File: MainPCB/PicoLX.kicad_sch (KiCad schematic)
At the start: 57 parts, among them J1 USB_C_Receptacle_USB2.0, SW1 SW_Push, U1 RP2040, U2 W25Q32JVSS, U3 NCP1117-3.3_SOT223, Y1 12.000MHz

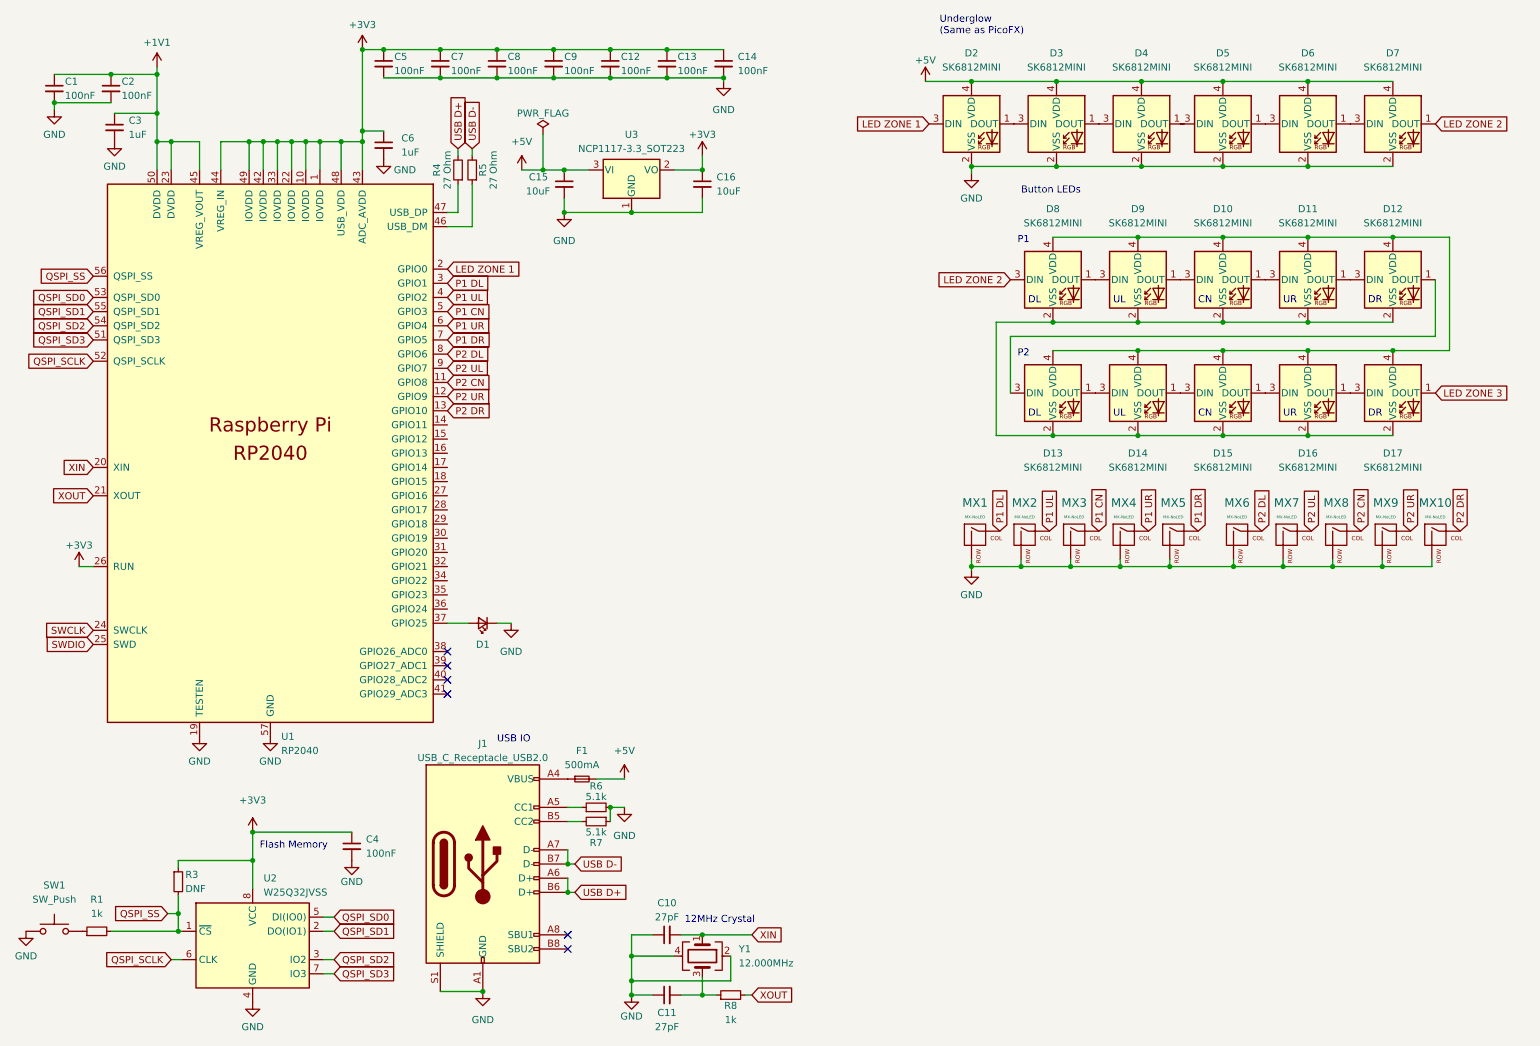
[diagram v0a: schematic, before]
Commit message: Route switches, begin routing LEDs
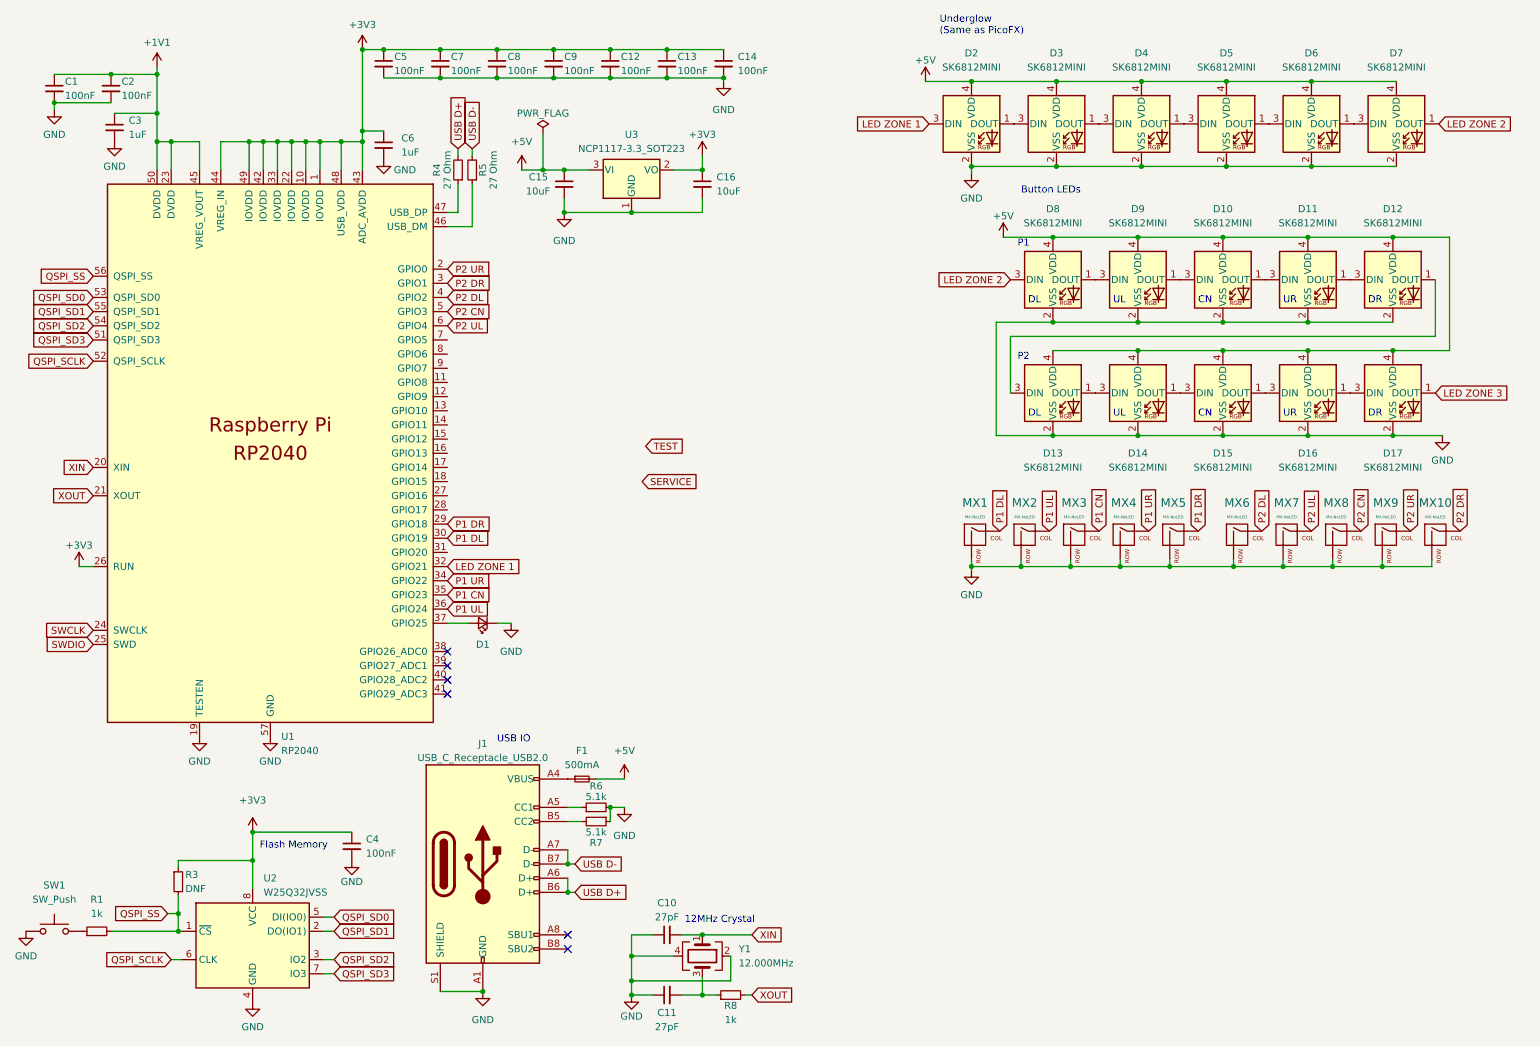
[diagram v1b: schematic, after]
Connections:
- net +5V: now also D10.4 (VDD), D11.4 (VDD), D12.4 (VDD), D13.4 (VDD), D14.4 (VDD), D15.4 (VDD), D16.4 (VDD), D17.4 (VDD), D8.4 (VDD), D9.4 (VDD)
- net GND: now also D10.2 (VSS), D11.2 (VSS), D12.2 (VSS), D13.2 (VSS), D14.2 (VSS), D15.2 (VSS), D16.2 (VSS), D17.2 (VSS), D8.2 (VSS), D9.2 (VSS)
- net LED ZONE 1: now also U1.32 (GPIO21); no longer U1.2 (GPIO0)
- net P1 CN: now also U1.35 (GPIO23); no longer U1.5 (GPIO3)
- net P1 DL: now also U1.30 (GPIO19); no longer U1.3 (GPIO1)
- net P1 DR: now also U1.29 (GPIO18); no longer U1.7 (GPIO5)
- net P1 UL: now also U1.36 (GPIO24); no longer U1.4 (GPIO2)
- net P1 UR: now also U1.34 (GPIO22); no longer U1.6 (GPIO4)
- net P2 CN: now also U1.5 (GPIO3); no longer U1.11 (GPIO8)
- net P2 DL: now also U1.4 (GPIO2); no longer U1.8 (GPIO6)
- net P2 DR: now also U1.3 (GPIO1); no longer U1.13 (GPIO10)
- net P2 UL: now also U1.6 (GPIO4); no longer U1.9 (GPIO7)
- net P2 UR: now also U1.2 (GPIO0); no longer U1.12 (GPIO9)
- net at D5.3 (DIN): now also D4.1 (DOUT)
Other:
- moved on the sheet: D5, D6, D7

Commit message: Final functional routing
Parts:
- added C17: 100nF, Capacitor_SMD:C_0402_1005Metric_Pad0.74x0.62mm_HandSolder, symbol Device:C_Small
- added C18, C19, C20, C21, C22, C23, C24, C25, C26, C27, C28, C29, C30, C31, C32, C33, C34, C35, C36: 100uF, Capacitor_SMD:C_0402_1005Metric_Pad0.74x0.62mm_HandSolder, symbol Device:C_Small
- added D18, D19, D20: SK6812MINI, marbastlib-various:LED_6028R, symbol LED:SK6812MINI
- added U4: SN74LV1T34DBV, Package_TO_SOT_SMD:SOT-23-5, symbol Logic_LevelTranslator:SN74LV1T34DBV
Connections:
- net +5V: now also C17.2, C18.2, C19.2, C20.2, C21.2, C22.2, C23.2, C24.1, C25.1, C26.1, C27.1, C28.1, C29.2, C30.2, C31.2, C32.2, C33.2, C34.2, C35.2, C36.2, D18.4 (VDD), D19.4 (VDD), D20.4 (VDD), U4.5 (VCC)
- net GND: now also C17.1, C18.1, C19.1, C20.1, C21.1, C22.1, C23.1, C24.2, C25.2, C26.2, C27.2, C28.2, C29.1, C30.1, C31.1, C32.1, C33.1, C34.1, C35.1, C36.1, D18.2 (VSS), D19.2 (VSS), D20.2 (VSS), U4.3 (GND)
- net LED ZONE 1: now also U4.4 (Y); no longer U1.32 (GPIO21)
- net LED ZONE 2: now also D16.3 (DIN); no longer D8.3 (DIN)
- net LED ZONE 3: now also D9.1 (DOUT), D18.3 (DIN); no longer D17.1 (DOUT)
- net at D10.3 (DIN): now also D12.1 (DOUT); no longer D9.1 (DOUT)
- net at D15.1 (DOUT): now also D13.3 (DIN); no longer D16.3 (DIN)
- net at D14.1 (DOUT): now also D11.3 (DIN); no longer D15.3 (DIN)
- net at D10.1 (DOUT): now also D8.3 (DIN); no longer D11.3 (DIN)
- new net: D15.3 (DIN), D17.1 (DOUT)
- new net: D18.1 (DOUT), D19.3 (DIN)
- new net: D19.1 (DOUT), D20.3 (DIN)
- new net LED SIGNAL: U1.32 (GPIO21), U4.2 (A)
- no-connect marks 6 -> 7
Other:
- note added: "Middle 3 LEDs"
- note removed: "CN"
- note removed: "DL"
- note removed: "DR"
- note removed: "P1"
- note removed: "P2"
- note removed: "UL"
- note removed: "UR"
- moved on the sheet: D10, D11, D12, D13, D14, D15, D16, D17, D8, D9, MX1, MX10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

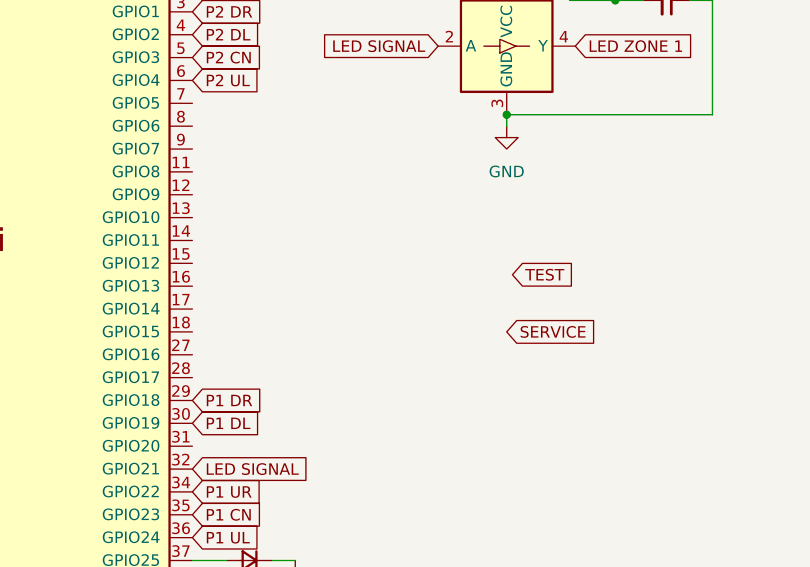
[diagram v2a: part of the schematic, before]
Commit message: Add test/service, update widths, fix DRC errors, etc
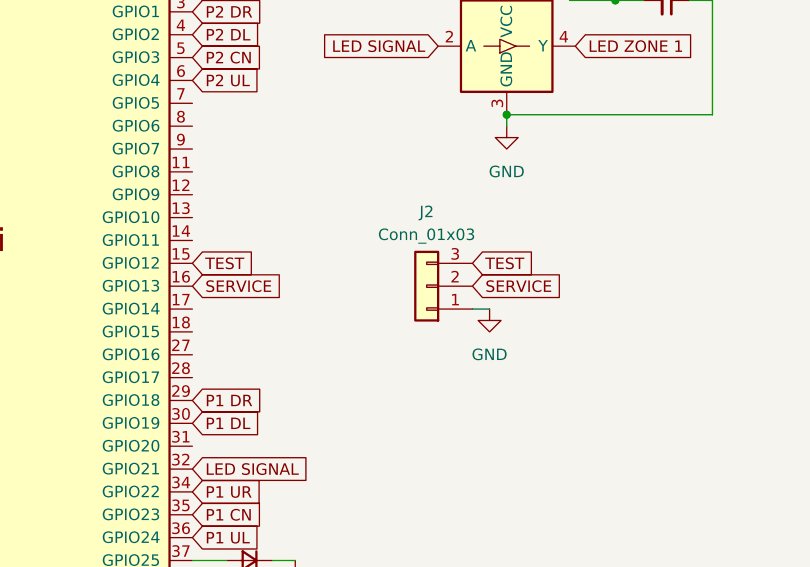
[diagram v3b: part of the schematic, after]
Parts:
- added J2: Conn_01x03, Connector_PinHeader_2.54mm:PinHeader_1x03_P2.54mm_Vertical, symbol Connector_Generic:Conn_01x03
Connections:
- net GND: now also J2.1 (Pin_1)
- net SERVICE: now also U1.16 (GPIO13), J2.2 (Pin_2)
- net TEST: now also U1.15 (GPIO12), J2.3 (Pin_3)
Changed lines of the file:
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@@
+    (stroke (width 0) (type default))
+  )
+  (wire (pts (xy 123.19 95.25) (xy 125.095 95.25))
     (stroke (width 0) (type default))
   )
@@
     )
   )
-  (global_label "SERVICE" (shape input) (at 127 97.79 0) (fields_autoplaced)
-    (effects (font (size 1.27 1.27)) (justify left))
-    (property "Intersheetrefs" "${INTERSHEET_REFS}" (at 137.6467 97.79 0)
+  (global_label "SERVICE" (shape input) (at 92.075 92.71 0) (fields_autoplaced)
+    (effects (font (size 1.27 1.27)) (justify left))
+    (property "Intersheetrefs" "${INTERSHEET_REFS}" (at 102.7217 92.71 0)
       (effects (font (size 1.27 1.27)) (justify left) hide)
     )
@@
     )
   )
-  (global_label "TEST" (shape input) (at 127.635 91.44 0) (fields_autoplaced)
-    (effects (font (size 1.27 1.27)) (justify left))
-    (property "Intersheetrefs" "${INTERSHEET_REFS}" (at 134.8345 91.44 0)
+  (global_label "TEST" (shape input) (at 92.075 90.17 0) (fields_autoplaced)
+    (effects (font (size 1.27 1.27)) (justify left))
+    (property "Intersheetrefs" "${INTERSHEET_REFS}" (at 99.2745 90.17 0)
       (effects (font (size 1.27 1.27)) (justify left) hide)
     )
@@
     )
   )
+  (global_label "TEST" (shape input) (at 123.19 90.17 0) (fields_autoplaced)
+    (effects (font (size 1.27 1.27)) (justify left))
+    (property "Intersheetrefs" "${INTERSHEET_REFS}" (at 130.3895 90.17 0)
+      (effects (font (size 1.27 1.27)) (justify left) hide)
+    )
+  )
   (global_label "XIN" (shape input) (at 28.575 95.25 180) (fields_autoplaced)
     (effects (font (size 1.27 1.27)) (justify right))
@@
     (property "Intersheetrefs" "${INTERSHEET_REFS}" (at 164.3291 33.655 0)
       (effects (font (size 1.27 1.27)) (justify right) hide)
+    )
+  )
+  (global_label "SERVICE" (shape input) (at 123.19 92.71 0) (fields_autoplaced)
+    (effects (font (size 1.27 1.27)) (justify left))
+    (property "Intersheetrefs" "${INTERSHEET_REFS}" (at 133.8367 92.71 0)
+      (effects (font (size 1.27 1.27)) (justify left) hide)
     )
   )
@@
     )
   )
+  (symbol (lib_id "Connector_Generic:Conn_01x03") (at 118.11 92.71 180) (unit 1)
+    (in_bom yes) (on_board yes) (dnp no) (fields_autoplaced)
+    (property "Reference" "J2" (at 118.11 84.455 0)
+      (effects (font (size 1.27 1.27)))
+    )
+    (property "Value" "Conn_01x03" (at 118.11 86.995 0)
+      (effects (font (size 1.27 1.27)))
+    )
+    (property "Footprint" "Connector_PinHeader_2.54mm:PinHeader_1x03_P2.54mm_Vertical" (at 118.11 92.71 0)
+      (effects (font (size 1.27 1.27)) hide)
+    )
+    (property "Datasheet" "~" (at 118.11 92.71 0)
+      (effects (font (size 1.27 1.27)) hide)
+    )
+    (pin "1")
+    (pin "2")
+    (pin "3")
+    (instances
+      (project "PicoLX"
+        (path "/c5e5d8b8-bebd-4318-85a6-adbafb95dd10"
+          (reference "J2") (unit 1)
+        )
+      )
+    )
+  )
   (symbol (lib_id "Device:C_Small") (at 251.46 16.51 0) (unit 1)
     (in_bom yes) (on_board yes) (dnp no)
@@
         )
       )
+    )
+  )
+  (symbol (lib_id "power:GND") (at 125.095 95.25 0) (unit 1)
+    (in_bom yes) (on_board yes) (dnp no) (fields_autoplaced)
+    (property "Reference" "#PWR034" (at 125.095 101.6 0)
+      (effects (font (size 1.27 1.27)) hide)
+    )
+    (property "Value" "GND" (at 125.095 100.33 0)
+      (effects (font (size 1.27 1.27)))
+    )
+    (property "Footprint" "" (at 125.095 95.25 0)
+      (effects (font (size 1.27 1.27)) hide)
+    )
+    (property "Datasheet" "" (at 125.095 95.25 0)
+      (effects (font (size 1.27 1.27)) hide)
+    )
+    (pin "1")
+    (instances
+      (project "PicoLX"
+        (path "/c5e5d8b8-bebd-4318-85a6-adbafb95dd10"
+          (reference "#PWR034") (unit 1)
+        )
+      )
+      (project "Panel"
+        (path "/f55927e3-6490-4e79-9229-dceeb24f0064"
+          (reference "#PWR015") (unit 1)
+        )
+      )
